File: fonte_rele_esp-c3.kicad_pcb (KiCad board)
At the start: 2 copper layers, 67.5 x 54.9 mm, 34 parts, among them J1 Screw_Terminal_01x02, J2 Conn_01x05_Pin, J3 Screw_Terminal_01x03, K1 G5LE-1, Q1 AO3400A, U1 AZ1117CH2-3.3, U2 HS-40012, U3 ESP32-C3-WROOM-02

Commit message: Atualiza esquematico, PCB e gerbers
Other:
- board text added: "COM | NF | NA"
- board text added: "NA NF COM"
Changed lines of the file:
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@@
 			(crossoutdnponfab yes)
 			(subtractmaskfromsilk no)
-			(outputformat 1)
+			(outputformat 4)
 			(mirror no)
-			(drillshape 1)
+			(drillshape 0)
 			(scaleselection 1)
-			(outputdirectory "")
+			(outputdirectory "GERBER_PROT1/")
 		)
 	)
@@
 		(sheetname "/")
 		(sheetfile "fonte_rele_esp-c3.kicad_sch")
-		(units
-			(unit
-				(name "A")
-				(pins "1" "2" "3")
-			)
-		)
 		(attr through_hole)
 		(duplicate_pad_numbers_are_jumpers no)
@@
 		)
 		(fp_line
-			(start 11 -4.3)
-			(end 11 -3.3)
-			(stroke
-				(width 0.12)
-				(type solid)
-			)
-			(layer "F.SilkS")
-		)
-		(fp_line
-			(start 9 -4.3)
-			(end 11 -4.3)
-			(stroke
-				(width 0.12)
-				(type solid)
-			)
-			(layer "F.SilkS")
-		)
-		(fp_line
-			(start 6 -4.3)
-			(end 6 -3.3)
-			(stroke
-				(width 0.12)
-				(type solid)
-			)
-			(layer "F.SilkS")
-		)
-		(fp_line
-			(start 4 -4.3)
-			(end 6 -4.3)
-			(stroke
-				(width 0.12)
-				(type solid)
-			)
-			(layer "F.SilkS")
-		)
-		(fp_line
-			(start 1 -4.3)
-			(end 1 -3.3)
-			(stroke
-				(width 0.12)
-				(type solid)
-			)
-			(layer "F.SilkS")
-		)
-		(fp_line
-			(start -1 -4.3)
-			(end 1 -4.3)
-			(stroke
-				(width 0.12)
-				(type solid)
-			)
-			(layer "F.SilkS")
-		)
-		(fp_line
-			(start 11 -3.3)
-			(end 9 -3.3)
-			(stroke
-				(width 0.12)
-				(type solid)
-			)
-			(layer "F.SilkS")
-		)
-		(fp_line
-			(start 9 -3.3)
-			(end 9 -4.3)
-			(stroke
-				(width 0.12)
-				(type solid)
-			)
-			(layer "F.SilkS")
-		)
-		(fp_line
-			(start 6 -3.3)
-			(end 4 -3.3)
-			(stroke
-				(width 0.12)
-				(type solid)
-			)
-			(layer "F.SilkS")
-		)
-		(fp_line
-			(start 4 -3.3)
-			(end 4 -4.3)
-			(stroke
-				(width 0.12)
-				(type solid)
-			)
-			(layer "F.SilkS")
-		)
-		(fp_line
-			(start 1 -3.3)
-			(end -1 -3.3)
-			(stroke
-				(width 0.12)
-				(type solid)
-			)
-			(layer "F.SilkS")
-		)
-		(fp_line
-			(start -1 -3.3)
-			(end -1 -4.3)
-			(stroke
-				(width 0.12)
-				(type solid)
-			)
-			(layer "F.SilkS")
-		)
-		(fp_line
-			(start -2.62 -2.3)
-			(end 12.62 -2.3)
-			(stroke
-				(width 0.12)
-				(type solid)
-			)
-			(layer "F.SilkS")
-		)
-		(fp_line
-			(start -2.62 2)
-			(end 12.62 2)
-			(stroke
-				(width 0.12)
-				(type solid)
-			)
-			(layer "F.SilkS")
-		)
-		(fp_line
 			(start -2.62 3.5)
 			(end 12.62 3.5)
@@
 		)
 		(fp_line
-			(start -2.5 -2.3)
-			(end 12.5 -2.3)
-			(stroke
-				(width 0.1)
-				(type solid)
-			)
-			(layer "F.Fab")
-		)
-		(fp_line
 			(start 10.955 -1.138)
 			(end 8.862 0.955)
@@
 			(layer "F.Fab")
 		)
-		(fp_rect
-			(start 9 -4.3)
-			(end 11 -3.3)
-			(stroke
-				(width 0.1)
-				(type solid)
-			)
-			(fill no)
-			(layer "F.Fab")
-		)
-		(fp_rect
-			(start 4 -4.3)
-			(end 6 -3.3)
-			(stroke
-				(width 0.1)
-				(type solid)
-			)
-			(fill no)
-			(layer "F.Fab")
-		)
-		(fp_rect
-			(start -1 -4.3)
-			(end 1 -3.3)
-			(stroke
-				(width 0.1)
-				(type solid)
-			)
-			(fill no)
-			(layer "F.Fab")
-		)
 		(fp_circle
 			(center 10 0)
@@
 	)
 	(gr_rect
+		(start 108.45 109.65)
+		(end 112.625 114.25)
+		(stroke
+			(width 0.1)
+			(type default)
+		)
+		(fill no)
+		(layer "B.SilkS")
+	)
+	(gr_rect
+		(start 108.45 114.25)
+		(end 112.625 119.725)
+		(stroke
+			(width 0.1)
+			(type solid)
+		)
+		(fill no)
+		(layer "B.SilkS")
+	)
+	(gr_rect
+		(start 108.45 119.725)
+		(end 112.625 124.075)
+		(stroke
+			(width 0.1)
+			(type default)
+		)
+		(fill no)
+		(layer "B.SilkS")
+	)
+	(gr_rect
 		(start 105.5 83.25)
 		(end 173 138.1506)
@@
 		)
 	)
-	(gr_text "+3V3"
-		(at 105.8 109 270)
+	(gr_text "COM | NF | NA"
+		(at 106.075 108.825 270)
 		(layer "F.SilkS" knockout)
 		(effects
 			(font
-				(size 0.762 0.762)
-				(thickness 0.1905)
+				(size 1.27 1.27)
+				(thickness 0.254)
 				(bold yes)
 			)
@@
 		)
 	)
+	(gr_text "NA  NF  COM"
+		(at 106.625 122.5 270)
+		(layer "B.SilkS" knockout)
+		(effects
+			(font
+				(size 1.27 1.27)
+				(thickness 0.254)
+				(bold yes)
+			)
+			(justify left bottom mirror)
+		)
+	)

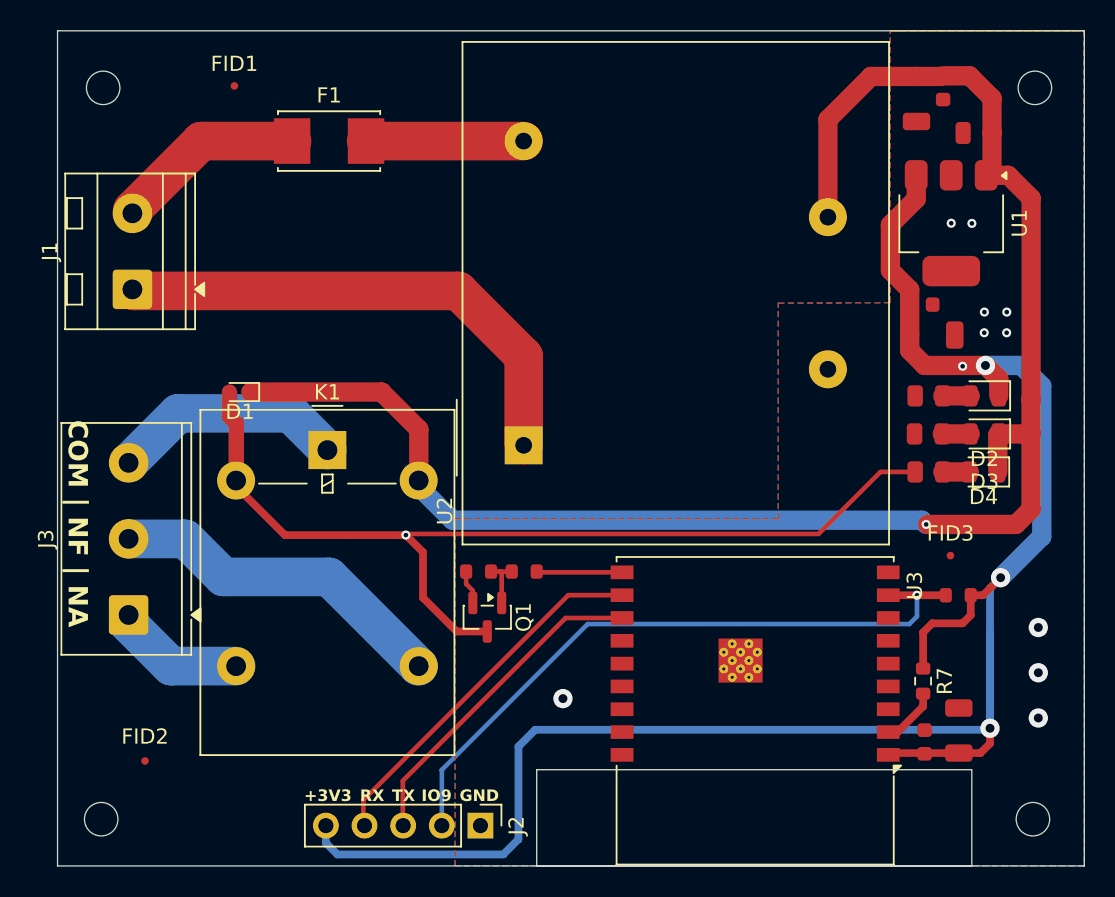
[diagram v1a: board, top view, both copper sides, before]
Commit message: Atualiza projeto KiCad e imagens da PCB
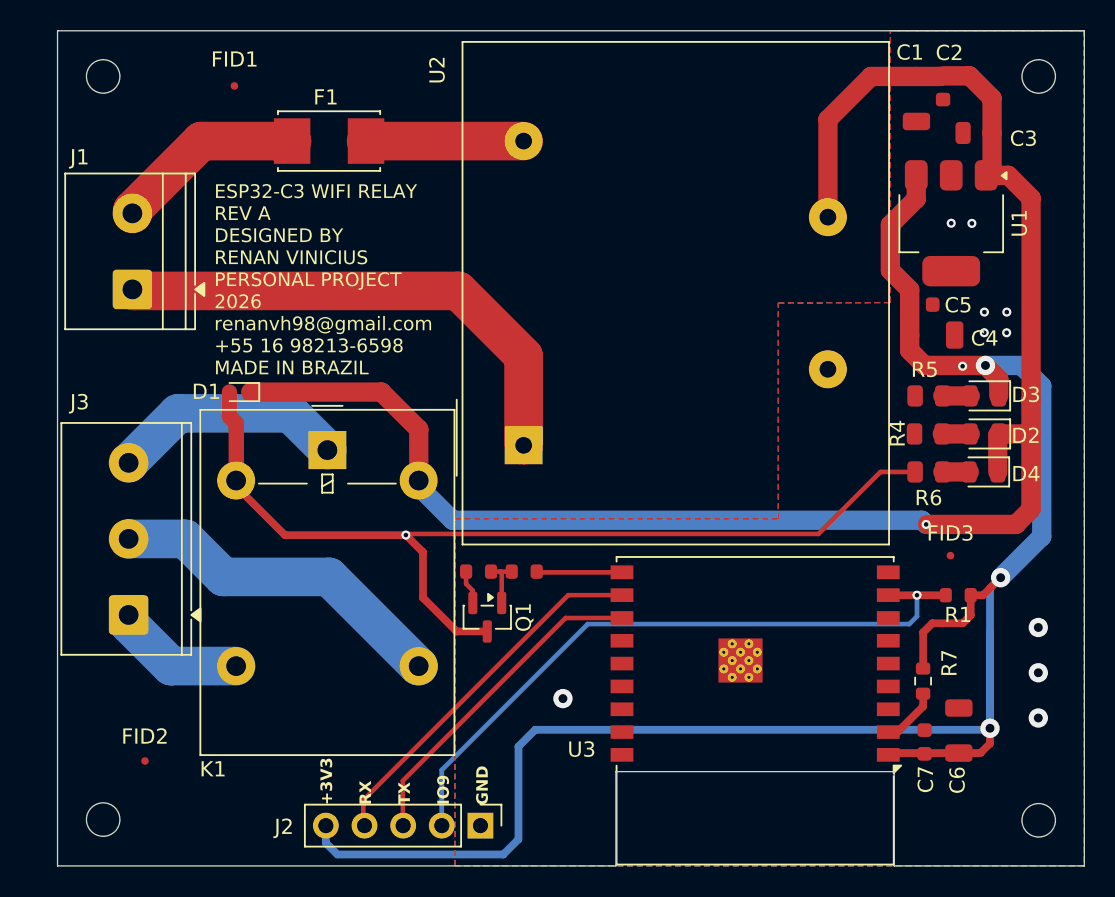
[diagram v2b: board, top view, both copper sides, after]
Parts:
- added G***: LOGO, LOGO, B.Cu at (124.3, 96.5)
- moved H3 0.79 mm to (170.0, 86.2)
- moved H2 0.75 mm to (108.5, 86.2)
- moved H1 0.39 mm to (170.0, 135.2)
- moved H4 0.13 mm to (108.5, 135.1)
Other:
- outline, holes or cut-outs redrawn
- board text added: "ESP32-C3 WIFI RELAY REV A DESIGNED BY RENAN VINICIUS PERSONAL PROJECT 2026 renanvh98@gmail.com +55 16 98213-6598 MADE IN BRAZIL"
- board text added: "N | L"
- board text added: "NA|NF|COM"
- board text removed: "COM | NF | NA"
- board text removed: "NA NF COM"
